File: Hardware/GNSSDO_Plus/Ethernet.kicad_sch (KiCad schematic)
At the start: 31 parts, among them J5 MagJack_PoE, U4 KSZ8041NL/I

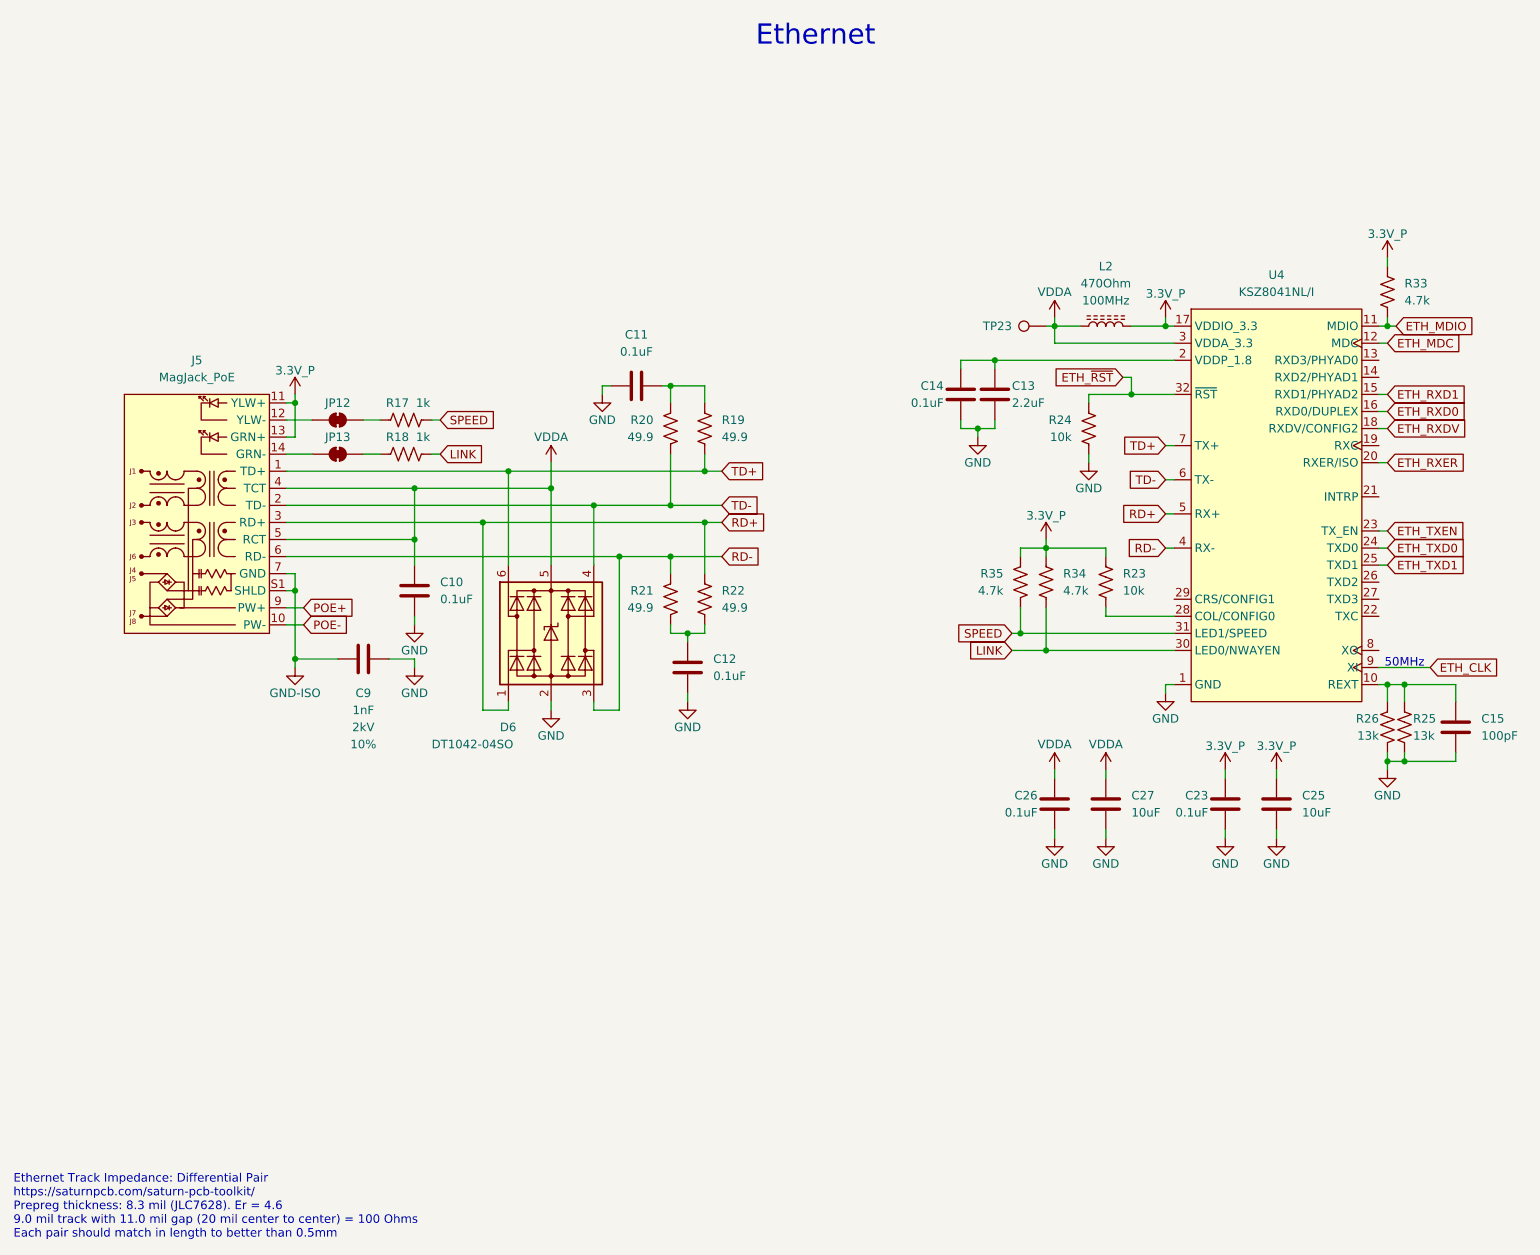
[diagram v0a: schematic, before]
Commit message: GNSSDO+ : update symbols and footprints
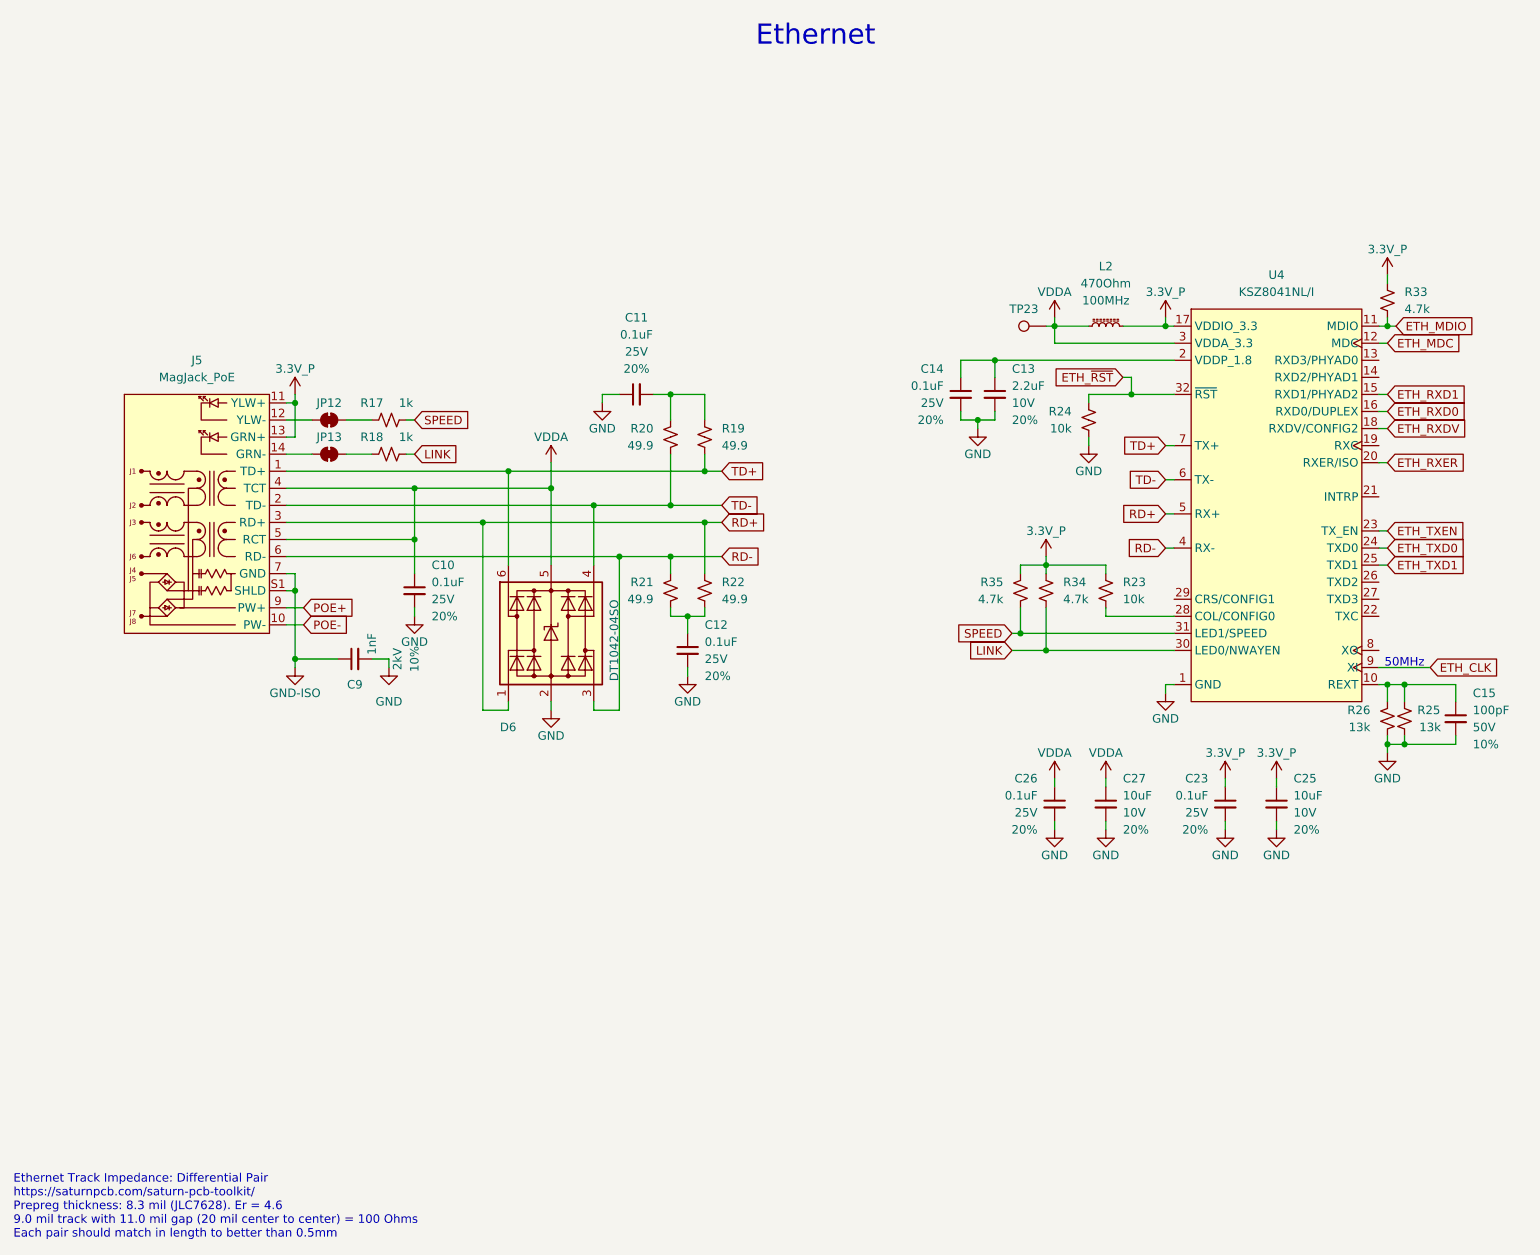
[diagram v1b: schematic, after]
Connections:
- net 3.3V_P: now also R23.1, R33.2, R34.2, R35.2; no longer R23.2, R33.1, R34.1, R35.1
- net ETH_MDIO: now also R33.1; no longer R33.2
- net ETH_~{RST}: now also R24.2; no longer R24.1
- net GND: now also R24.1, R25.1, R26.1; no longer R24.2, R25.2, R26.2
- net LINK: now also R18.2, R34.1; no longer R18.1, R34.2
- net RD+: now also R22.2; no longer R22.1
- net RD-: now also R21.2; no longer R21.1
- net SPEED: now also R17.2, R35.1; no longer R17.1, R35.2
- net TD+: now also R19.1; no longer R19.2
- net TD-: now also R20.1; no longer R20.2
- net at C15.1, U4.10 (REXT): now also R25.2, R26.2; no longer R25.1, R26.1
- net at JP13.2 (B): now also R18.1; no longer R18.2
- net at U4.28 (COL/CONFIG0): now also R23.2; no longer R23.1
- net at JP12.2 (B): now also R17.1; no longer R17.2
- new net: C12.1, R21.1, R22.1
- new net: C11.2, R19.2, R20.2
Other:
- moved on the sheet: C11, C12, C15, C9, JP12, JP13

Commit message: GNSSDO Plus - ready for review
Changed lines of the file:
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@@
 		(on_board yes)
 		(dnp no)
+		(fields_autoplaced yes)
 		(property "Reference" "C9"
 			(at 67.3163 116.84 90)
@@
 		)
 		(property "Value" "1nF"
-			(at 69.85 112.395 0)
+			(at 67.3163 119.38 90)
 			(effects
 				(font
 					(size 1.27 1.27)
 				)
-				(justify left)
 			)
 		)
@@
 		)
 		(property "Voltage" "2kV"
-			(at 73.66 113.03 0)
+			(at 67.3163 121.92 90)
 			(effects
 				(font
@@
 		)
 		(property "Tolerance" "10%"
-			(at 76.2 113.03 0)
+			(at 67.3163 124.46 90)
 			(effects
 				(font

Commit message: GNSSDO+ v02 PCB - with DP5305 PoE module, PowerPath Controllers and MS8607 PHT sensor
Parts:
- D6: symbol SparkFun-DiscreteSemi:D_TVS_ESD_USB -> SparkFun-DiscreteSemi:D_TVS_ESD_USB_5V; Rating (none) -> 5VWM/9VC
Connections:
- no-connect marks 0 -> 9
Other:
- title: Ethernet -> GNSSDO Plus - Ethernet

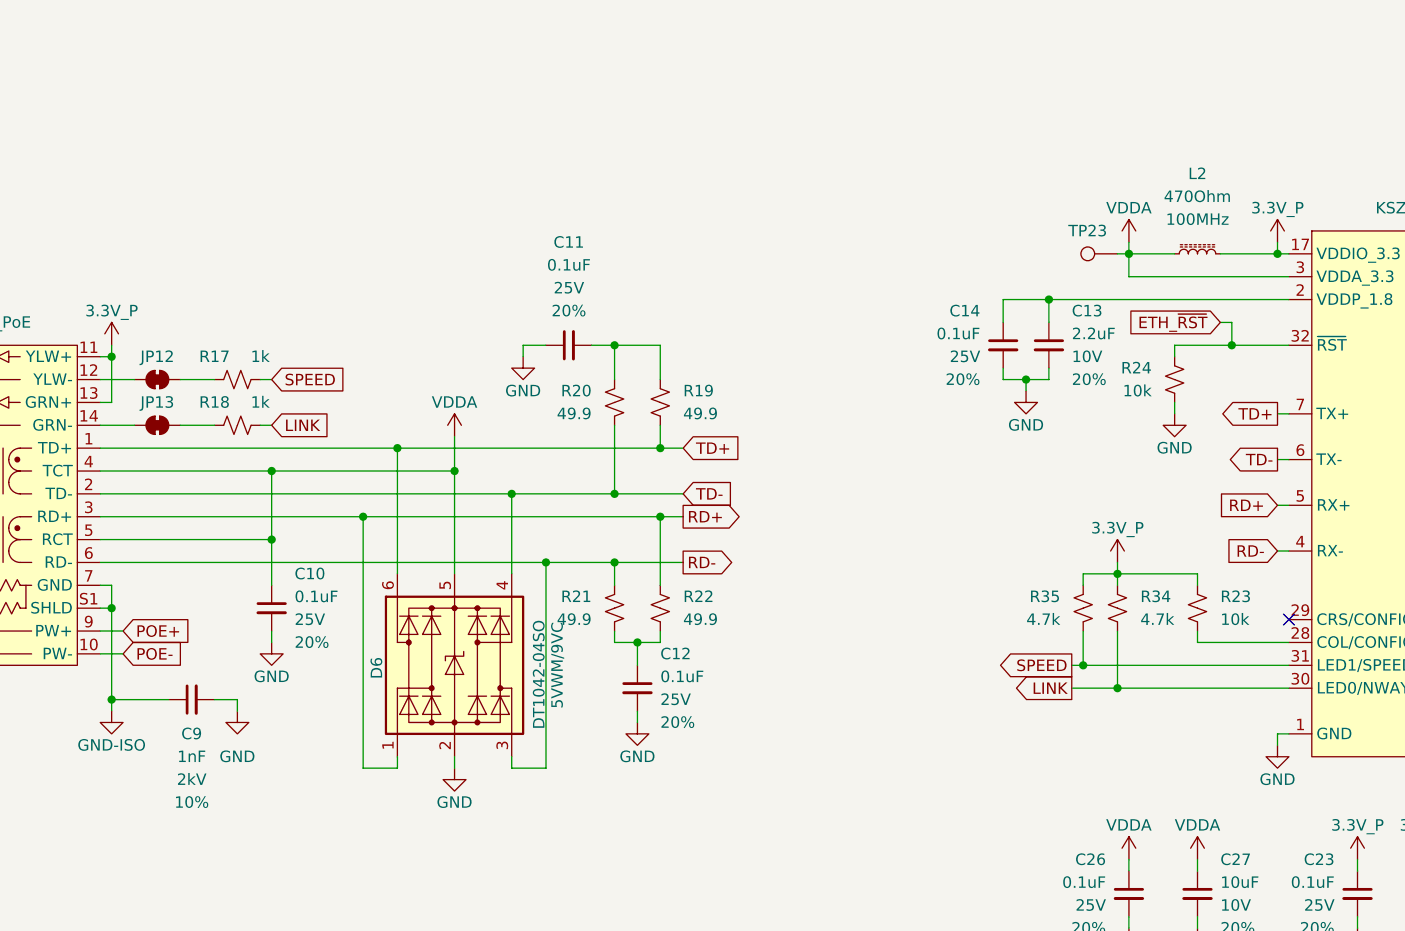
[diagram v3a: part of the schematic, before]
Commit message: Update GNSSDO KiCad files to match latest SparkFun library
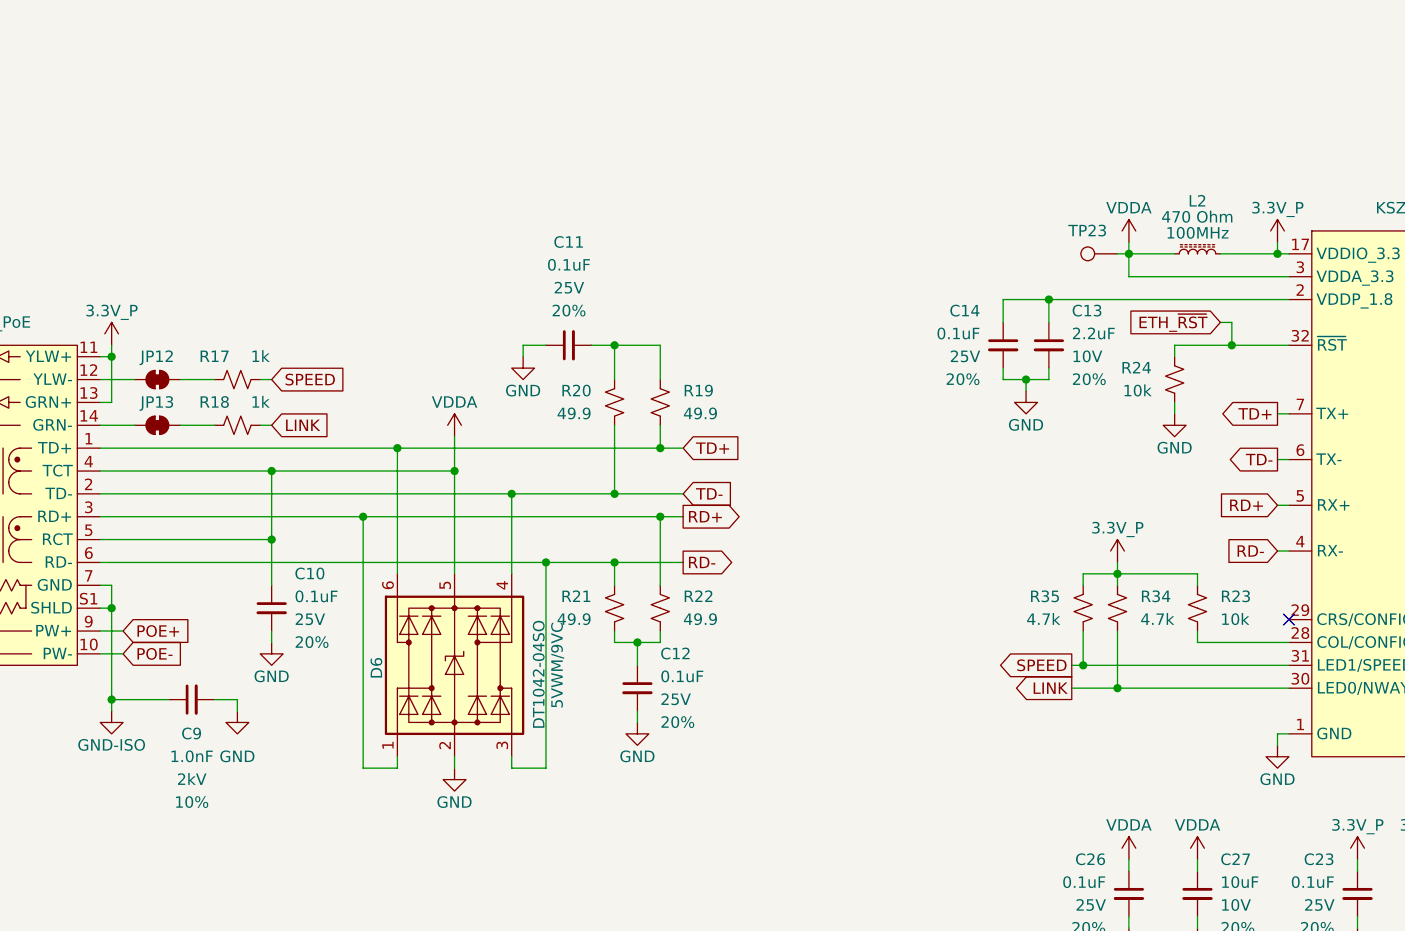
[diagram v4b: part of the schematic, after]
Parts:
- C13: PROD_ID CAP-07888 -> CAP-24999
- C9: value 1nF -> 1.0nF
- J5: symbol SparkFun-Connector:MagJack_PoE_RJ45 -> SparkFun-Connector:RJ45_MagJack_PoE
- L2: value 470Ohm -> 470 Ohm; symbol SparkFun-Coil:470Ohm_0603_1.0A -> SparkFun-Coil:Ferrite_470Ohm_0603_1.0A
- TP23: footprint SparkFun-Connector:1x01 -> SparkFun-Connector:1x01_P2.54mm
